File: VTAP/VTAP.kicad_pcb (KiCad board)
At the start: 2 copper layers, 68 x 171.5 mm, 42 parts, among them J1 MX 52901-0274

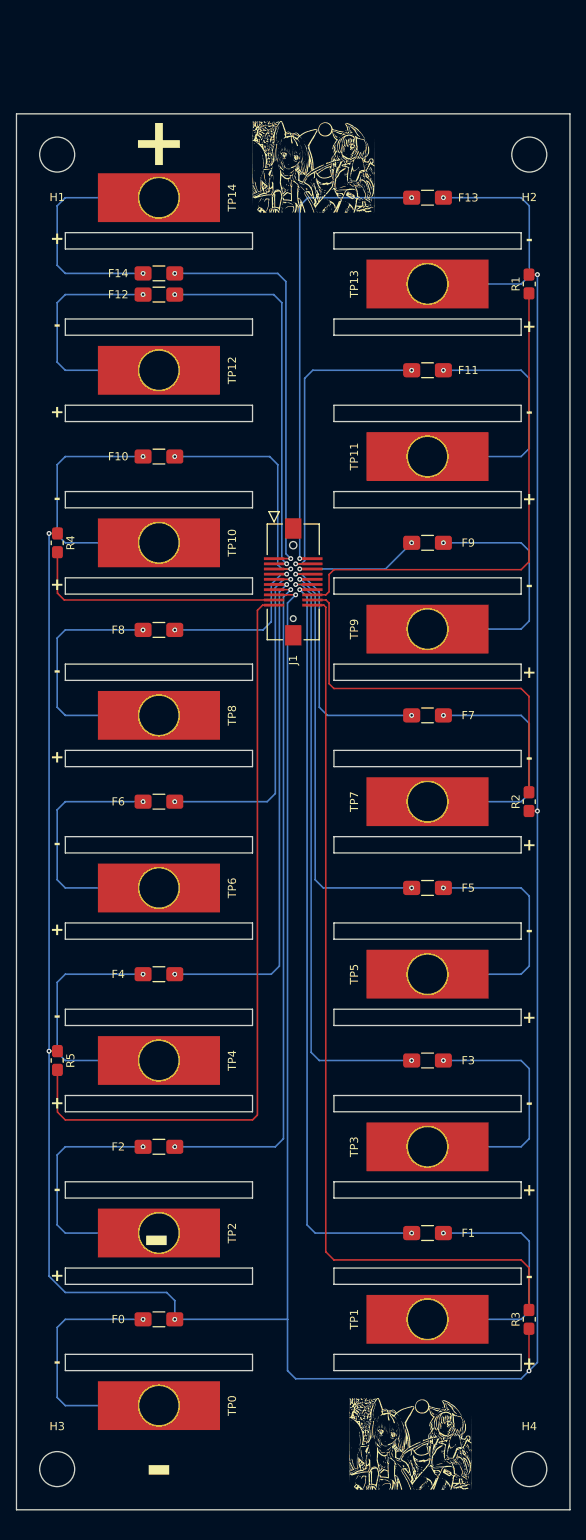
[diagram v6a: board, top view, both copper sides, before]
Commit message: vtap pcb traces adjusted to avoid shorting
thermistor pads moved further from test points
traces adjusted to be further from edge cuts
fuses rearranged to avoid needing two fuses in close proximity
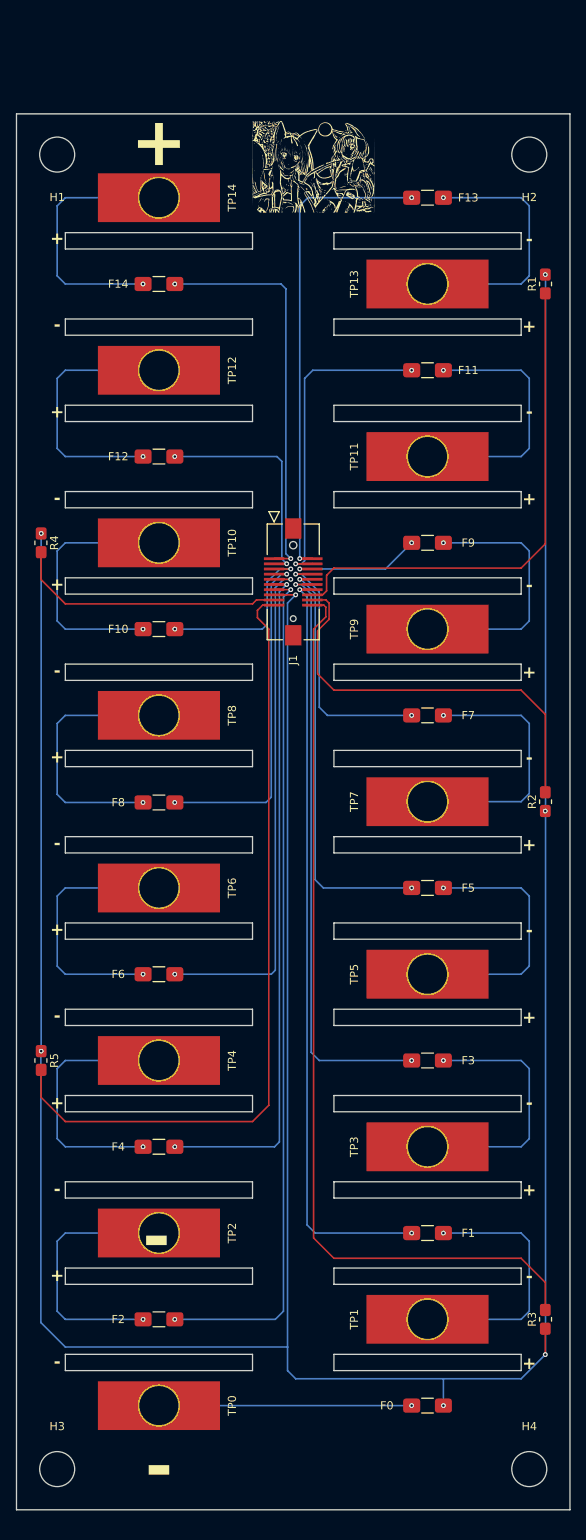
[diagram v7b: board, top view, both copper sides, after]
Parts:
- removed the G*** at (104.4, 204.4)
- moved F0 34.7 mm to (106.5, 199.7)
- moved F4 21.2 mm to (73.5, 167.9)
- moved F10 21.2 mm to (73.5, 104.3)
- moved F2 21.2 mm to (73.5, 189.1)
- moved F6 21.2 mm to (73.5, 146.7)
- moved F8 21.2 mm to (73.5, 125.6)
- moved F12 19.9 mm to (73.5, 83.1)
- moved R1 2.00 mm to (121.0, 61.9)
- moved R2 2.00 mm to (121.0, 125.5)
- moved R3 2.00 mm to (121.0, 189.1)
- moved R4 2.00 mm to (59.0, 93.7)
- moved R5 2.00 mm to (59.0, 157.3)
- moved F14 1.30 mm to (73.5, 61.9)
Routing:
- net /TP6: track 42.4 -> 63.9 mm
- net /TP4: track 62.1 -> 83.5 mm
- net /TP8: track 20.8 -> 42.2 mm
- net /TP2: track 83.6 -> 104.8 mm
- net /TP12: track 47.4 -> 27.8 mm
- net /TP10: track 29.2 -> 22.4 mm
- net /NTC5: track 94.7 -> 97.1 mm
- net /NTC3: track 111.9 -> 114.0 mm
- net GND: track 397.4 -> 399.4 mm
- net /NTC2: track 49.1 -> 51.1 mm
- net /NTC4: track 32.0 -> 33.4 mm
- net Net-(F0-Pad1): track 32.5 -> 31.0 mm
- net Net-(F14-Pad1): track 31.2 -> 32.5 mm
- net Net-(F12-Pad1): track 31.2 -> 32.5 mm
- net /TP14: track 50.4 -> 49.3 mm
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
